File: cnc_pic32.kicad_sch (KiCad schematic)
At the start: 0 parts

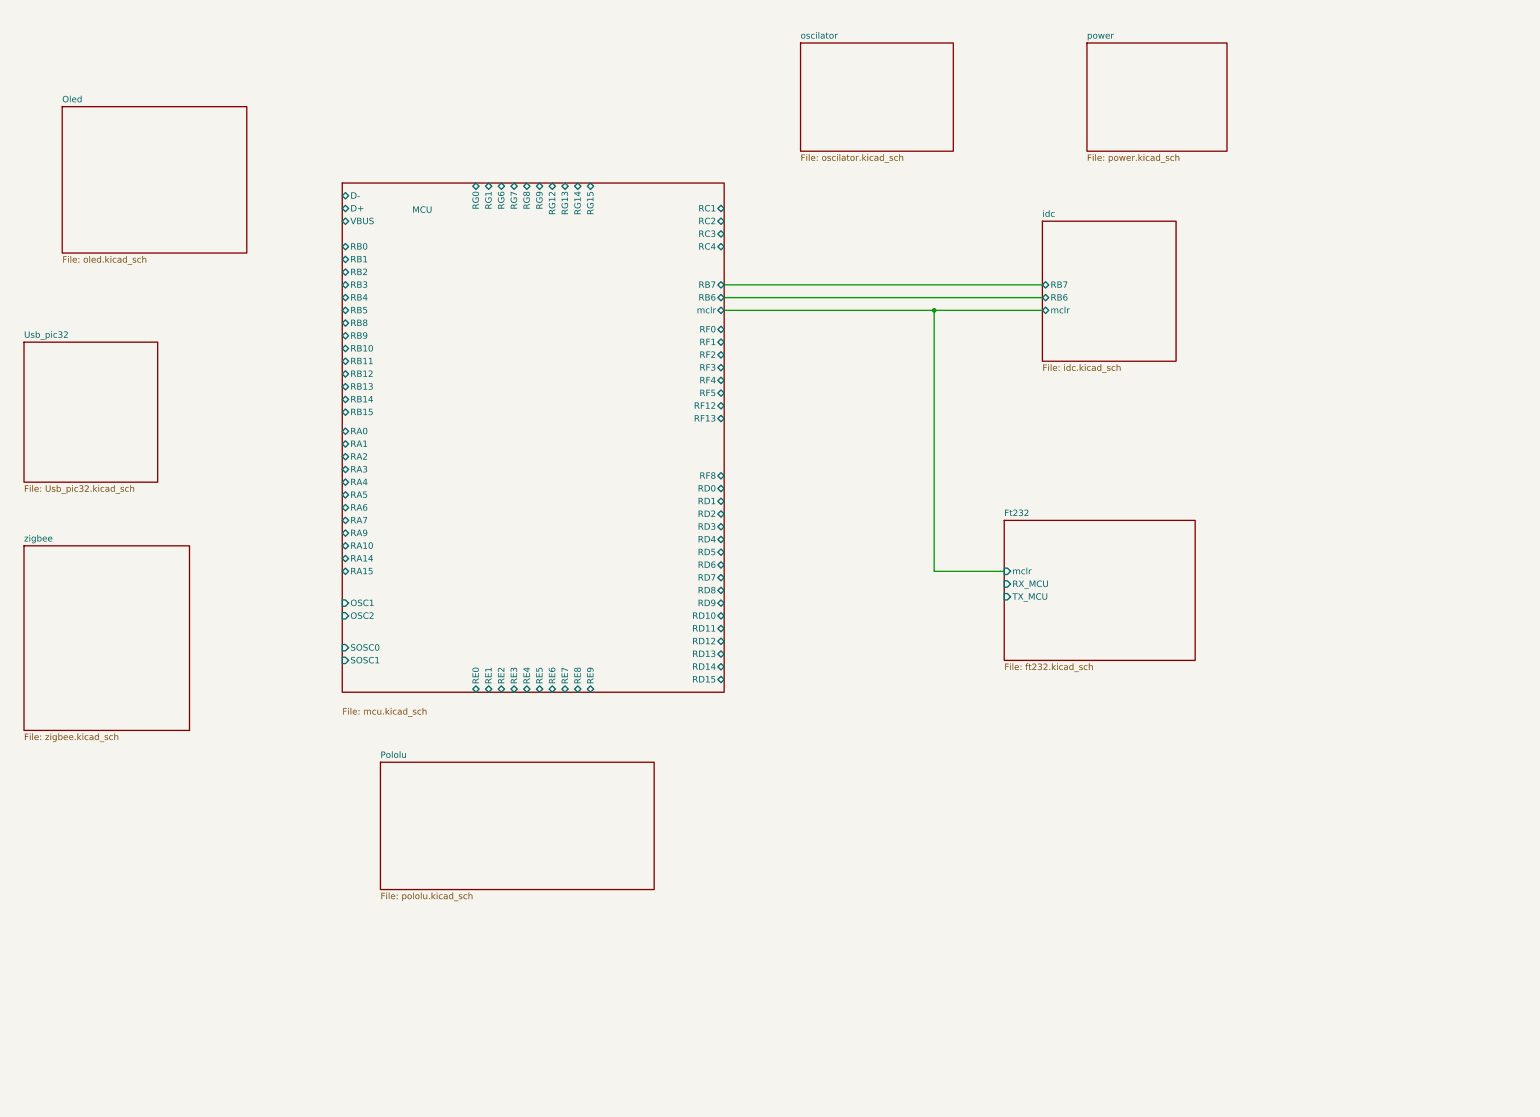
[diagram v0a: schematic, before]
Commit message: Fix Y1/J17 footprints, update PCB and schematics
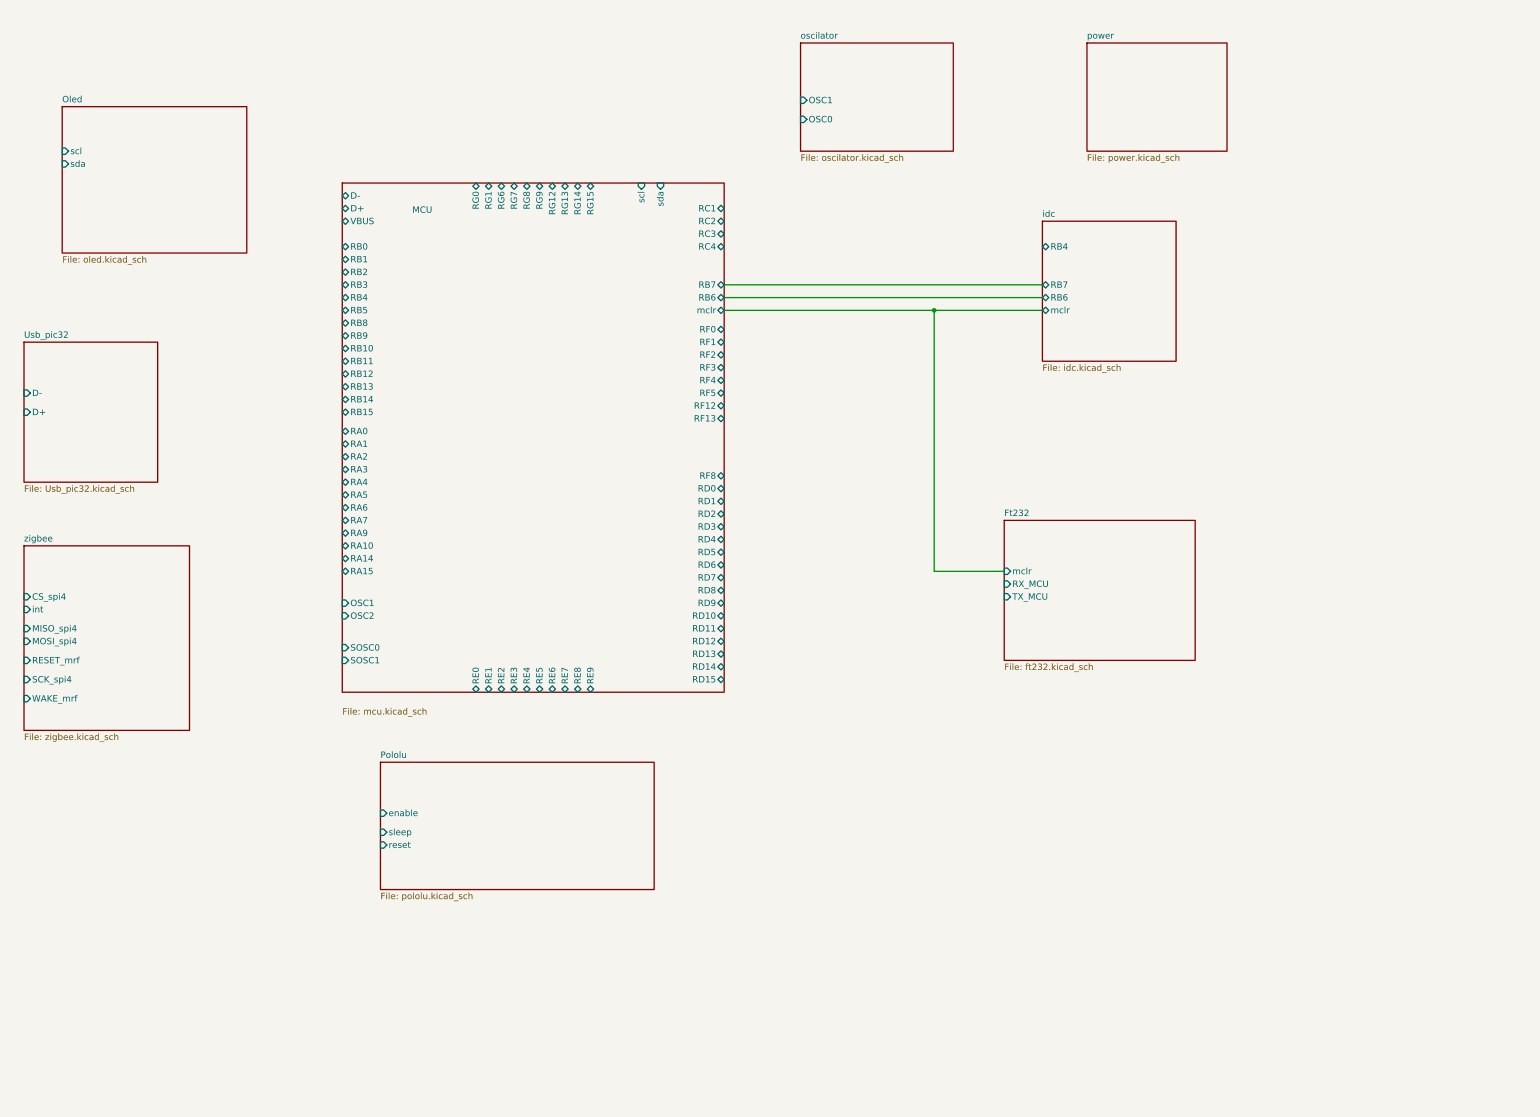
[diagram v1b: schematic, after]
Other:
- sheet MCU ports: added scl, sda; removed none
- sheet Oled ports: added scl, sda; removed none
- sheet Pololu ports: added enable, reset, sleep; removed none
- sheet Usb_pic32 ports: added D+, D-; removed none
- sheet idc ports: added RB4; removed none
- sheet oscilator ports: added OSC0, OSC1; removed none
- sheet zigbee ports: added CS_spi4, MISO_spi4, MOSI_spi4, RESET_mrf, SCK_spi4, WAKE_mrf, int; removed none
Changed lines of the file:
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@@
+			)
+		)
+		(pin "CS_spi4" input
+			(at 25.4 133.35 180)
+			(effects
+				(font
+					(size 1.27 1.27)
+				)
+				(justify left)
+			)
+		)
+		(pin "int" input
+			(at 25.4 135.89 180)
+			(effects
+				(font
+					(size 1.27 1.27)
+				)
+				(justify left)
+			)
+		)
+		(pin "MISO_spi4" input
+			(at 25.4 139.7 180)
+			(effects
+				(font
+					(size 1.27 1.27)
+				)
+				(justify left)
+			)
+		)
+		(pin "MOSI_spi4" input
+			(at 25.4 142.24 180)
+			(effects
+				(font
+					(size 1.27 1.27)
+				)
+				(justify left)
+			)
+		)
+		(pin "RESET_mrf" input
+			(at 25.4 146.05 180)
+			(effects
+				(font
+					(size 1.27 1.27)
+				)
+				(justify left)
+			)
+		)
+		(pin "SCK_spi4" input
+			(at 25.4 149.86 180)
+			(effects
+				(font
+					(size 1.27 1.27)
+				)
+				(justify left)
+			)
+		)
+		(pin "WAKE_mrf" input
+			(at 25.4 153.67 180)
+			(effects
+				(font
+					(size 1.27 1.27)
+				)
+				(justify left)
 			)
 		)
@@
 			)
 		)
+		(pin "RB4" bidirectional
+			(at 228.6 63.5 180)
+			(effects
+				(font
+					(size 1.27 1.27)
+				)
+				(justify left)
+			)
+		)
 		(instances
 			(project "cnc_pic32"
@@
 				)
 				(justify left)
+			)
+		)
+		(pin "scl" input
+			(at 148.59 50.8 90)
+			(effects
+				(font
+					(size 1.27 1.27)
+				)
+				(justify right)
+			)
+		)
+		(pin "sda" input
+			(at 152.4 50.8 90)
+			(effects
+				(font
+					(size 1.27 1.27)
+				)
+				(justify right)
 			)
 		)
@@
 			)
 		)
+		(pin "D+" input
+			(at 25.4 96.52 180)
+			(effects
+				(font
+					(size 1.27 1.27)
+				)
+				(justify left)
+			)
+		)
+		(pin "D-" input
+			(at 25.4 92.71 180)
+			(effects
+				(font
+					(size 1.27 1.27)
+				)
+				(justify left)
+			)
+		)
 		(instances
 			(project "cnc_pic32"
@@
 			)
 		)
+		(pin "scl" input
+			(at 33.02 44.45 180)
+			(effects
+				(font
+					(size 1.27 1.27)
+				)
+				(justify left)
+			)
+		)
+		(pin "sda" input
+			(at 33.02 46.99 180)
+			(effects
+				(font
+					(size 1.27 1.27)
+				)
+				(justify left)
+			)
+		)
 		(instances
 			(project "cnc_pic32"
@@
 			)
 		)
+		(pin "reset" input
+			(at 96.52 182.88 180)
+			(effects
+				(font
+					(size 1.27 1.27)
+				)
+				(justify left)
+			)
+		)
+		(pin "sleep" input
+			(at 96.52 180.34 180)
+			(effects
+				(font
+					(size 1.27 1.27)
+				)
+				(justify left)
+			)
+		)
+		(pin "enable" input
+			(at 96.52 176.53 180)
+			(effects
+				(font
+					(size 1.27 1.27)
+				)
+				(justify left)
+			)
+		)
 		(instances
 			(project "cnc_pic32"
@@
 			)
 		)
+		(pin "OSC0" input
+			(at 180.34 38.1 180)
+			(effects
+				(font
+					(size 1.27 1.27)
+				)
+				(justify left)
+			)
+		)
+		(pin "OSC1" input
+			(at 180.34 34.29 180)
+			(effects
+				(font
+					(size 1.27 1.27)
+				)
+				(justify left)
+			)
+		)

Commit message: feat: 25 hierarchical labels for 5 Pololus + fix J4/J15/J17/TP17 footprints + USB pin6→SH
- pololu.kicad_sch: 5→25 hierarchical labels (reset_N, sleep_N, enable_N, step_N, dir_N) with wires to each Pololu A4988
- pololu.kicad_sch: J17 footprint kiC:PinHeader → Library:PinHeader_1x06_P2.54mm_Vertical
- cnc_pic32.kicad_sch: expanded Pololu sheet box with 25 named sheet pins
- buttons.kicad_sch: all SW switches → Button_Switch_SMD:SW_SPST_CK_RS282G05A3
- tp_ft232.kicad_sch: kiC:pad_0508 + kiC:Pin_D1.5mmx1mm → Library:connector_pin1
- usb_conector_Ft232.kicad_sch: J4/J15 kiC:Pin_D1.5mmx1mm → Library:connector_pin1, J5 pin 6→SH
- Usb_pic32.kicad_sch: TP17 kiC:Pin_D1.5mmx1mm → Library:connector_pin1, J18 pin 6→SH
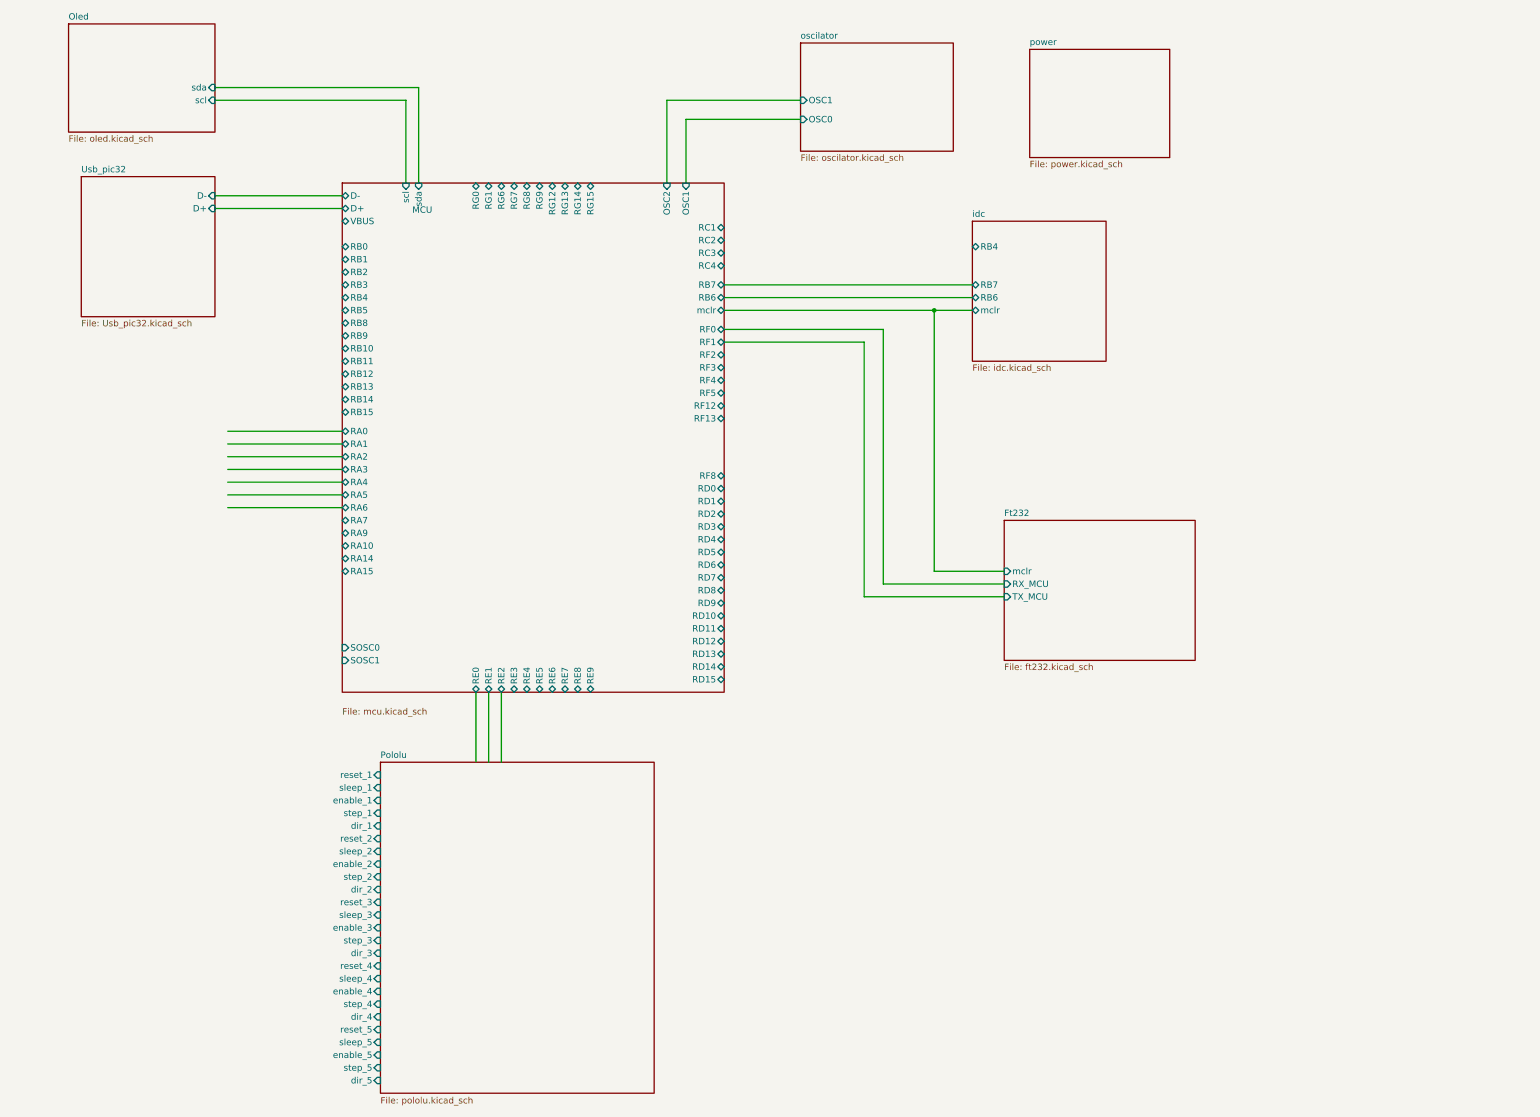
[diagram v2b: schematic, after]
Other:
- removed sheet zigbee
- sheet Pololu ports: added dir_1, dir_2, dir_3, dir_4, dir_5, enable_1, enable_2, enable_3, enable_4, enable_5, reset_1, reset_2, reset_3, reset_4, reset_5, sleep_1, sleep_2, sleep_3, sleep_4, sleep_5, step_1, step_2, step_3, step_4, step_5; removed enable, reset, sleep

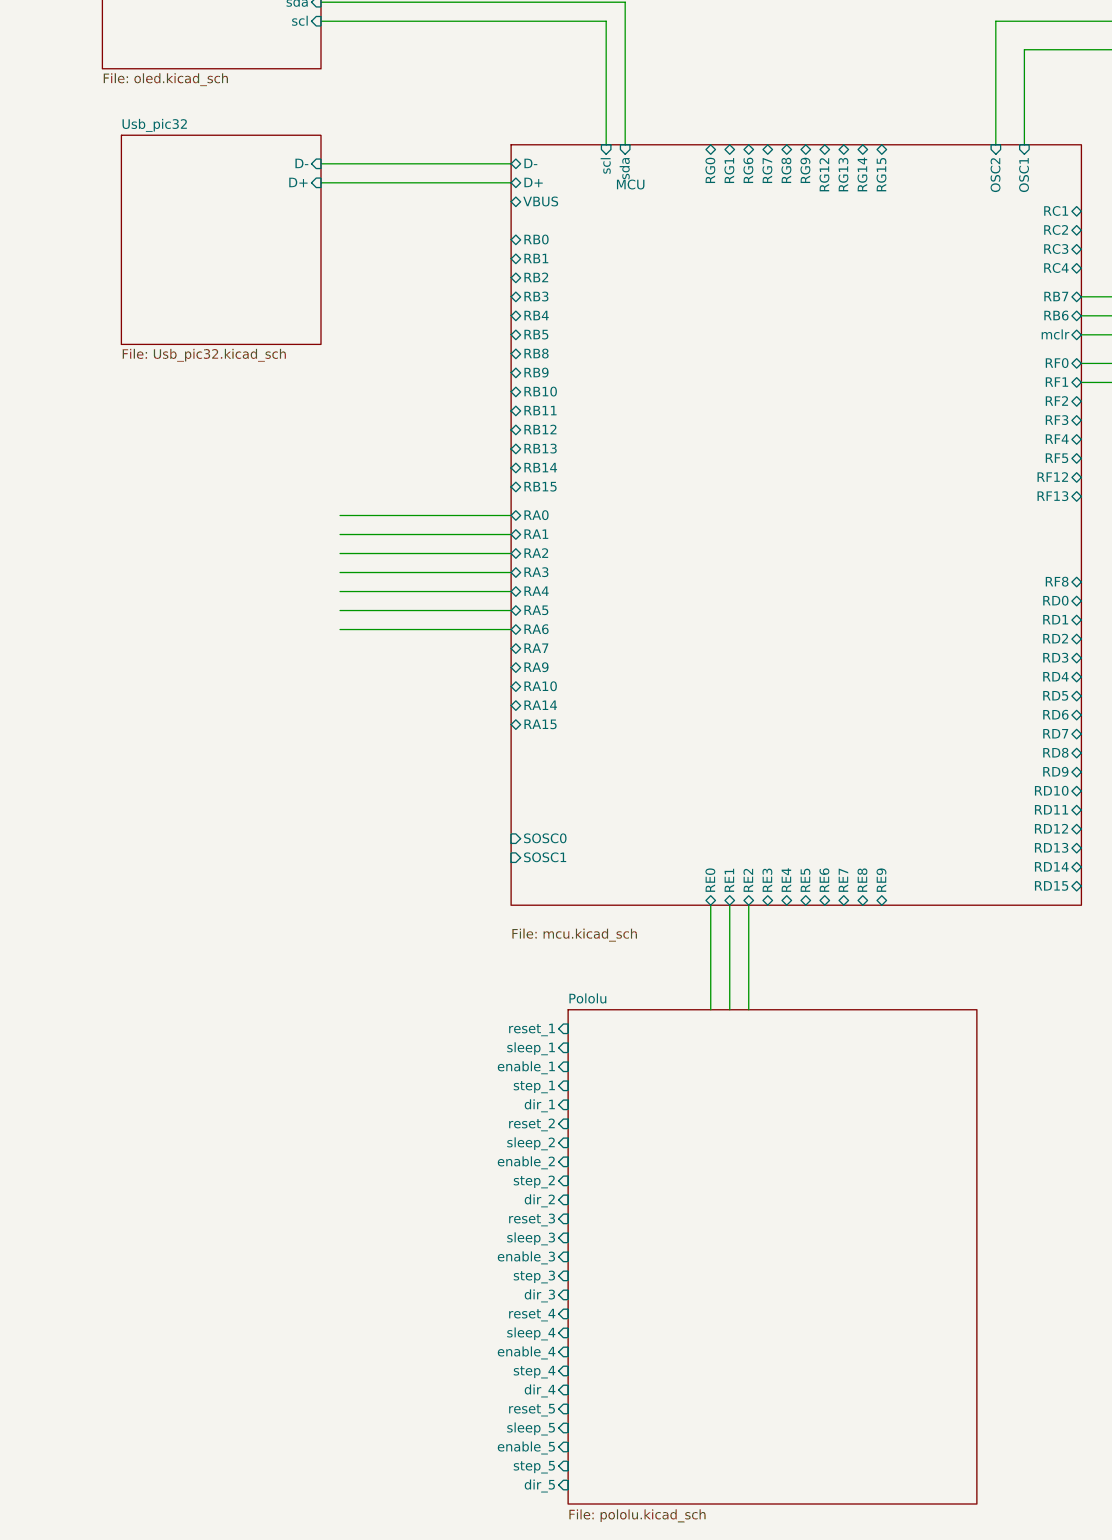
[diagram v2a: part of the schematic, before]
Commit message: fix: pololu.kicad_sch repair - restore A1-A5 symbols, fix dir_5 label, remove orphaned elements
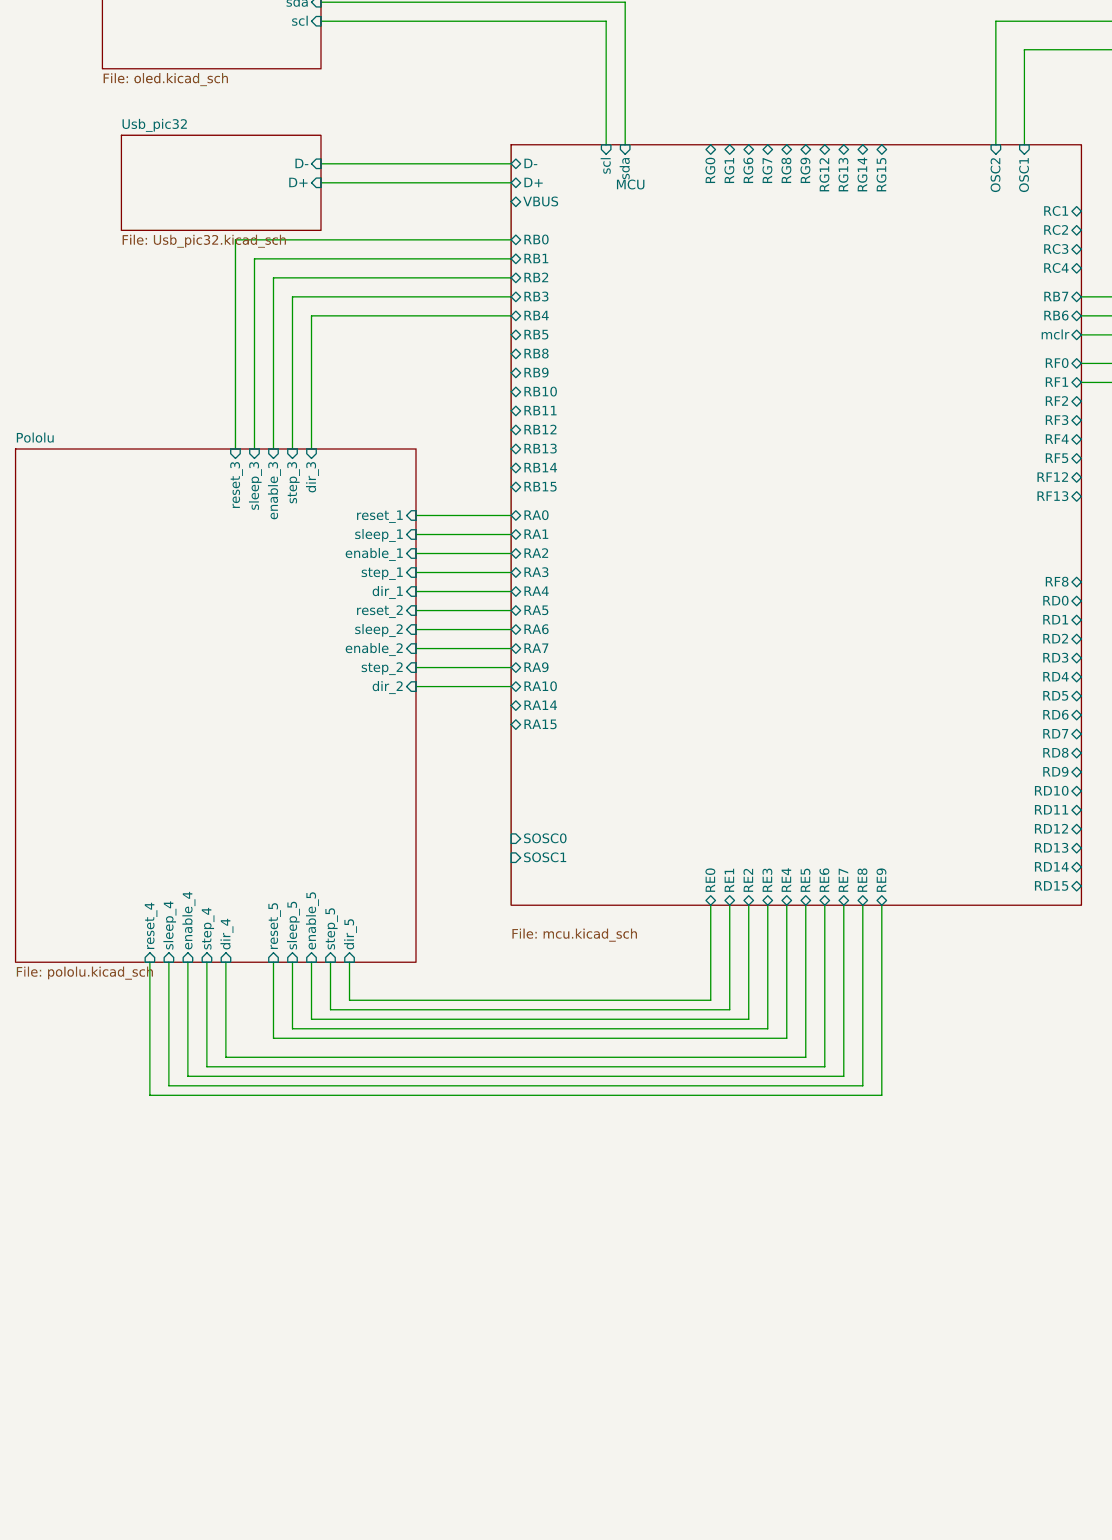
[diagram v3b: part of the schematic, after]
